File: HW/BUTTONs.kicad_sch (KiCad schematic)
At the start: 10 parts, among them SW1 SW_Push, SW2 SW_Push, SW3 SW_Push, SW4 SW_Push, SW5 SW_Push

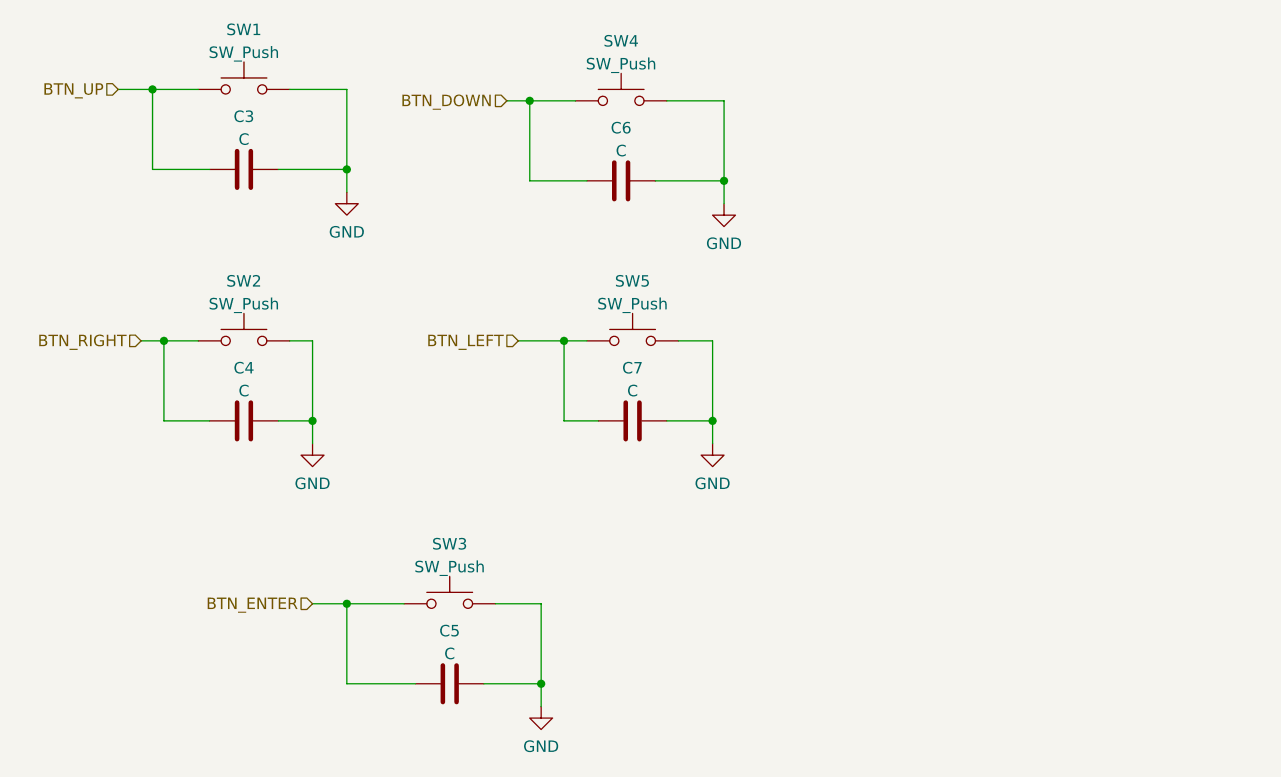
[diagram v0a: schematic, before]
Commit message: add capacitive touch buttons and converter AT42QT1070
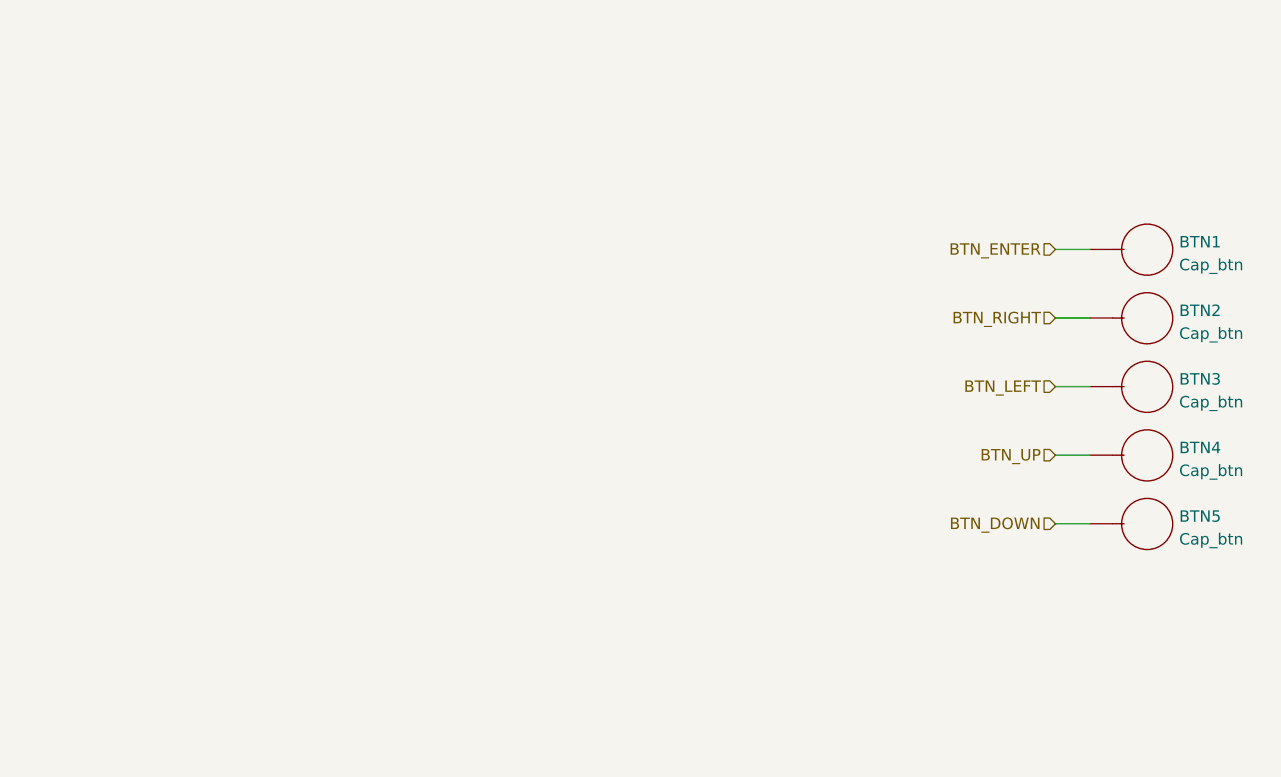
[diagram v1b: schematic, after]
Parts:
- removed C3, C4, C5, C6, C7: C, Capacitor_SMD:C_0603_1608Metric, symbol Device:C
- removed SW1, SW2, SW4, SW5: SW_Push, Button_Switch_SMD:SW_SPST_B3S-1000, symbol Switch:SW_Push
- removed SW3: SW_Push, Button_Switch_SMD:SW_SPST_TL3342, symbol Switch:SW_Push
- added BTN1, BTN2, BTN3, BTN4, BTN5: Cap_btn, Library:Cap_btn, symbol Library:Cap_btn
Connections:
- net BTN_DOWN: now also BTN5.
- net BTN_ENTER: now also BTN1.
- net BTN_LEFT: now also BTN3.
- net BTN_RIGHT: now also BTN2.
- net BTN_UP: now also BTN4.
